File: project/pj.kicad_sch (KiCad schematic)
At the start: 11 parts, among them J1 RPi_GPIO, J2 2B+, J3 zero, J4 3A+, J5 3B+, J6 4, J7 Conn_01x02, J8 Conn_01x02, SW1 SW_Push, SW2 SW_Push

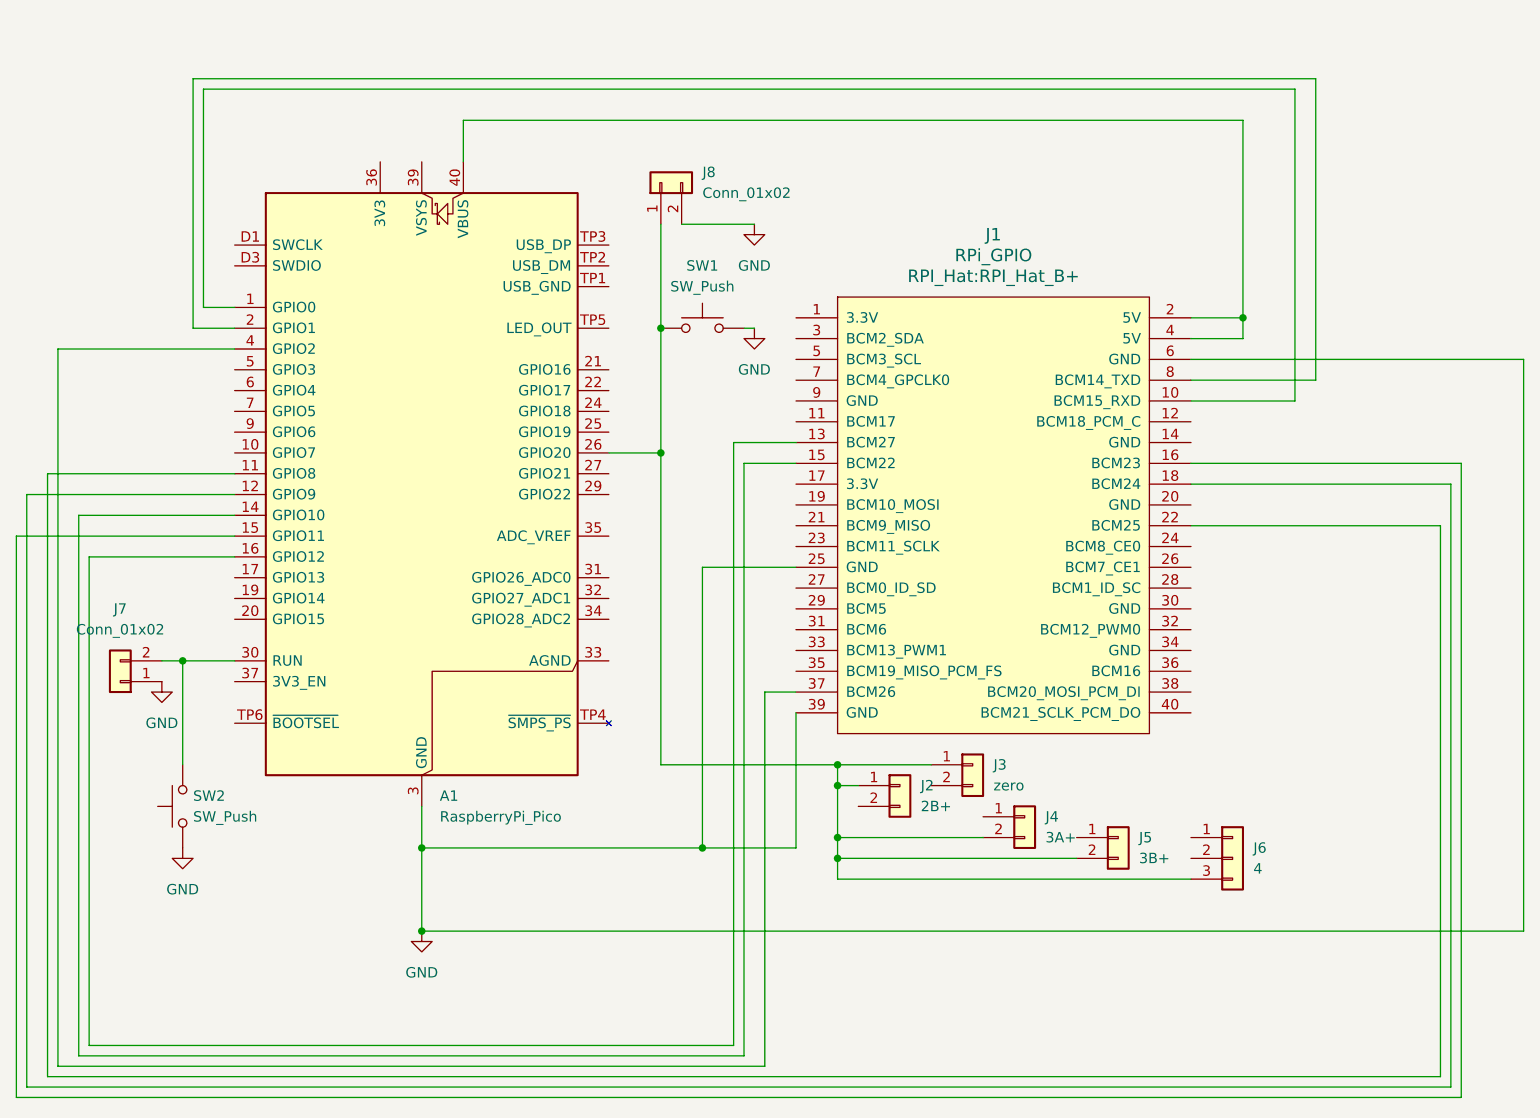
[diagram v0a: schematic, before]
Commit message: ground plane on both sides
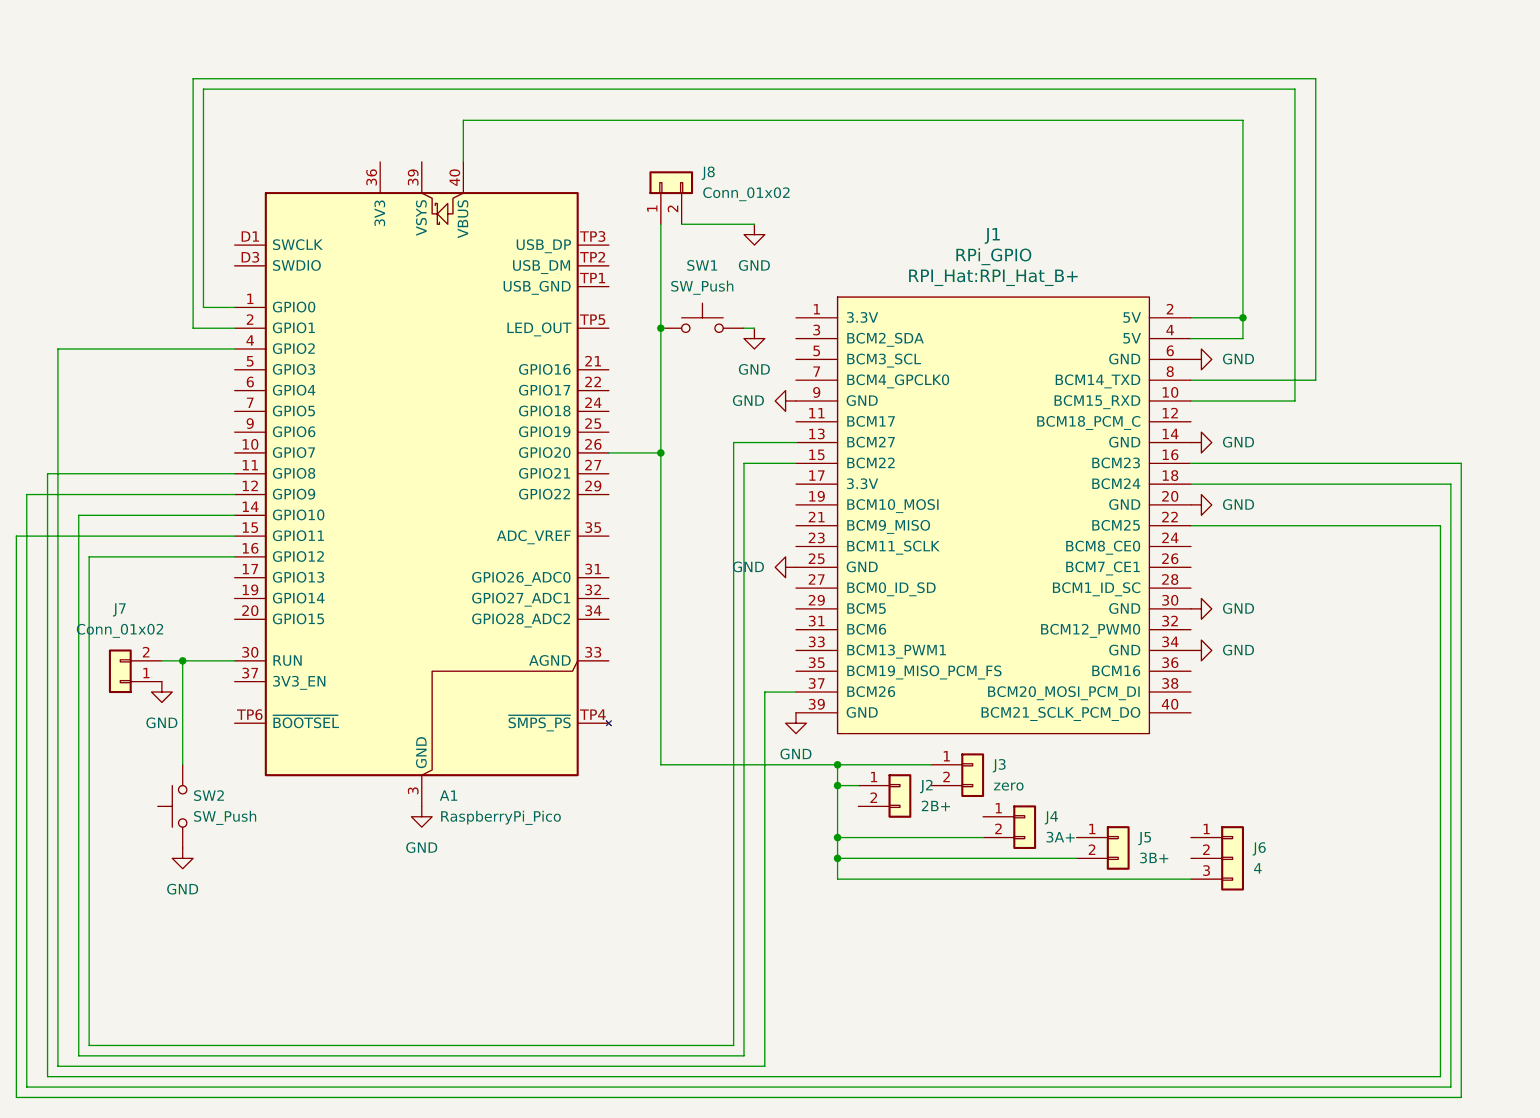
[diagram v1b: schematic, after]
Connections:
- net GND: now also J1.14 (GND), J1.20 (GND), J1.30 (GND), J1.34 (GND), J1.9 (GND)

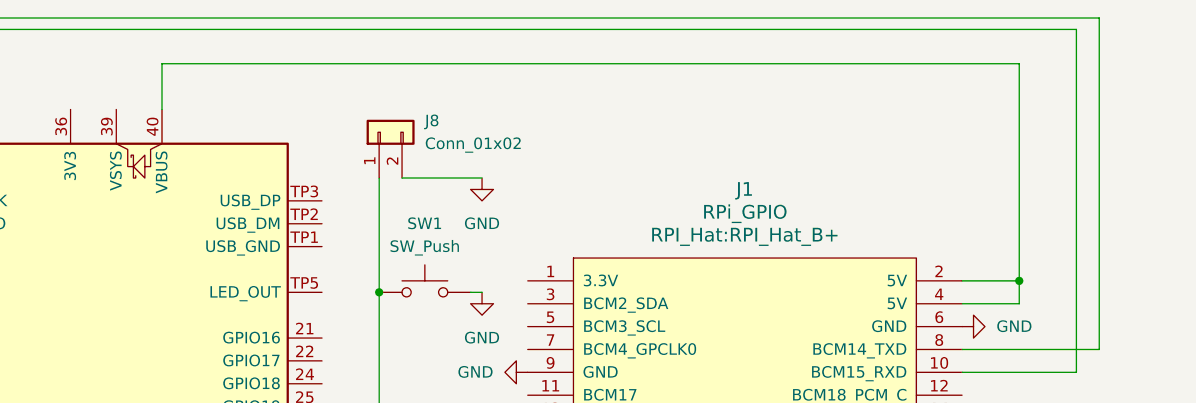
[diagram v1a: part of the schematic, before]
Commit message: Add Pico PWR and External PoWR
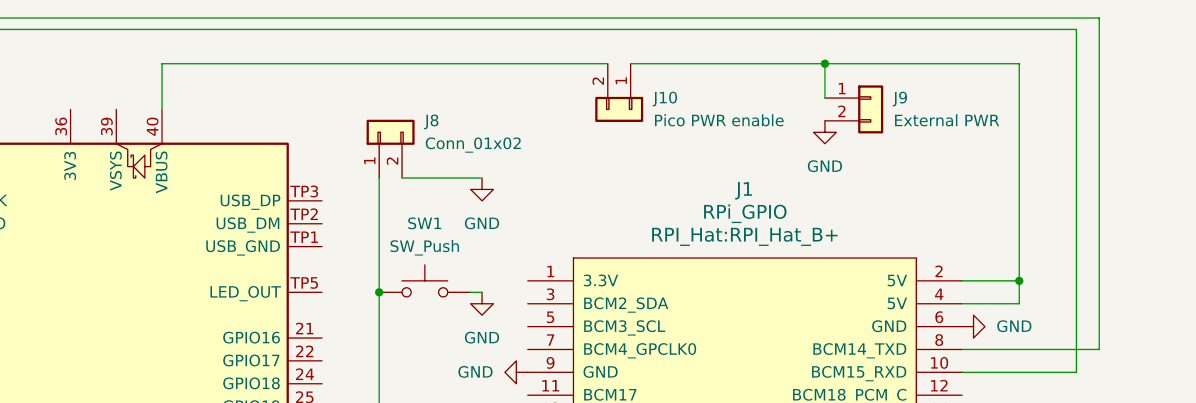
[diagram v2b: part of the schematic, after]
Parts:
- added J10: Pico PWR enable, symbol Connector_Generic:Conn_01x02
- added J9: External PWR, symbol Connector_Generic:Conn_01x02
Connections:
- net GND: now also J9.2 (Pin_2)
- net at J1.2 (5V), J1.4 (5V): now also J10.1 (Pin_1), J9.1 (Pin_1); no longer A1.40 (VBUS)
- new net: A1.40 (VBUS), J10.2 (Pin_2)
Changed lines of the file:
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@@
+	)
+	(junction
+		(at 165.1 31.75)
+		(diameter 0)
+		(color 0 0 0 0)
 	)
 	(junction
@@
 	(wire
 		(pts
+			(xy 165.1 35.56) (xy 165.1 31.75)
+		)
+		(stroke
+			(width 0)
+			(type default)
+		)
+	)
+	(wire
+		(pts
 			(xy 59.69 27.94) (xy 193.04 27.94)
 		)
@@
 	(wire
 		(pts
+			(xy 143.51 31.75) (xy 165.1 31.75)
+		)
+		(stroke
+			(width 0)
+			(type default)
+		)
+	)
+	(wire
+		(pts
 			(xy 38.1 77.47) (xy 63.5 77.47)
 		)
@@
 	(wire
 		(pts
+			(xy 165.1 31.75) (xy 186.69 31.75)
+		)
+		(stroke
+			(width 0)
+			(type default)
+		)
+	)
+	(wire
+		(pts
 			(xy 195.58 26.67) (xy 58.42 26.67)
 		)
@@
 	(wire
 		(pts
-			(xy 91.44 31.75) (xy 186.69 31.75)
+			(xy 91.44 31.75) (xy 140.97 31.75)
 		)
 		(stroke
@@
 	(symbol
 		(lib_id "power:GND")
+		(at 165.1 38.1 0)
+		(unit 1)
+		(exclude_from_sim no)
+		(in_bom yes)
+		(on_board yes)
+		(dnp no)
+		(fields_autoplaced yes)
+		(property "Reference" "#PWR014"
+			(at 165.1 44.45 0)
+			(effects
+				(font
+					(size 1.27 1.27)
+				)
+				(hide yes)
+			)
+		)
+		(property "Value" "GND"
+			(at 165.1 43.18 0)
+			(effects
+				(font
+					(size 1.27 1.27)
+				)
+			)
+		)
+		(property "Footprint" ""
+			(at 165.1 38.1 0)
+			(effects
+				(font
+					(size 1.27 1.27)
+				)
+				(hide yes)
+			)
+		)
+		(property "Datasheet" ""
+			(at 165.1 38.1 0)
+			(effects
+				(font
+					(size 1.27 1.27)
+				)
+				(hide yes)
+			)
+		)
+		(property "Description" "Power symbol creates a global label with name \"GND\" , ground"
+			(at 165.1 38.1 0)
+			(effects
+				(font
+					(size 1.27 1.27)
+				)
+				(hide yes)
+			)
+		)
+		(pin "1"
+		)
+		(instances
+			(project ""
+				(path "/3f830ea6-5a5f-4b7b-8d42-0620c39d4ee6"
+					(reference "#PWR014")
+					(unit 1)
+				)
+			)
+		)
+	)
+	(symbol
+		(lib_id "power:GND")
 		(at 57.15 120.65 0)
 		(unit 1)
@@
 	(symbol
 		(lib_id "Connector_Generic:Conn_01x02")
+		(at 170.18 35.56 0)
+		(unit 1)
+		(exclude_from_sim no)
+		(in_bom yes)
+		(on_board yes)
+		(dnp no)
+		(fields_autoplaced yes)
+		(property "Reference" "J9"
+			(at 172.72 35.5599 0)
+			(effects
+				(font
+					(size 1.27 1.27)
+				)
+				(justify left)
+			)
+		)
+		(property "Value" "External PWR"
+			(at 172.72 38.0999 0)
+			(effects
+				(font
+					(size 1.27 1.27)
+				)
+				(justify left)
+			)
+		)
+		(property "Footprint" ""
+			(at 170.18 35.56 0)
+			(effects
+				(font
+					(size 1.27 1.27)
+				)
+				(hide yes)
+			)
+		)
+		(property "Datasheet" "~"
+			(at 170.18 35.56 0)
+			(effects
+				(font
+					(size 1.27 1.27)
+				)
+				(hide yes)
+			)
+		)
+		(property "Description" "Generic connector, single row, 01x02, script generated (kicad-library-utils/schlib/autogen/connector/)"
+			(at 170.18 35.56 0)
+			(effects
+				(font
+					(size 1.27 1.27)
+				)
+				(hide yes)
+			)
+		)
+		(pin "1"
+		)
+		(pin "2"
+		)
+		(instances
+			(project ""
+				(path "/3f830ea6-5a5f-4b7b-8d42-0620c39d4ee6"
+					(reference "J9")
+					(unit 1)
+				)
+			)
+		)
+	)
+	(symbol
+		(lib_id "Connector_Generic:Conn_01x02")
 		(at 115.57 39.37 90)
 		(unit 1)
@@
 					(unit 1)
 				)
+			)
+		)
+	)
+	(symbol
+		(lib_id "Connector_Generic:Conn_01x02")
+		(at 143.51 36.83 270)
+		(unit 1)
+		(exclude_from_sim no)
+		(in_bom yes)
+		(on_board yes)
+		(dnp no)
+		(fields_autoplaced yes)
+		(property "Reference" "J10"
+			(at 146.05 35.5599 90)
+			(effects
+				(font
+					(size 1.27 1.27)
+				)
+				(justify left)
+			)
+		)
+		(property "Value" "Pico PWR enable"
+			(at 146.05 38.0999 90)
+			(effects
+				(font
+					(size 1.27 1.27)
+				)
+				(justify left)
+			)
+		)
+		(property "Footprint" ""
+			(at 143.51 36.83 0)
+			(effects
+				(font
+					(size 1.27 1.27)
+				)
+				(hide yes)
+			)
+		)
+		(property "Datasheet" "~"
+			(at 143.51 36.83 0)
+			(effects
+				(font
+					(size 1.27 1.27)
+				)
+				(hide yes)
+			)
+		)
+		(property "Description" "Generic connector, single row, 01x02, script generated (kicad-library-utils/schlib/autogen/connector/)"
+			(at 143.51 36.83 0)
+			(effects
+				(font
+					(size 1.27 1.27)
+				)
+				(hide yes)
+			)
+		)
+		(pin "2"
+		)
+		(pin "1"
+		)
+		(instances
+			(project ""
+				(path "/3f830ea6-5a5f-4b7b-8d42-0620c39d4ee6"
+					(reference "J10")
+					(unit 1)
+				)

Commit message: pwr eneble
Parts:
- J10: footprint (none) -> Jumper:SolderJumper-2_P1.3mm_Bridged2Bar_Pad1.0x1.5mm
- J9: footprint (none) -> Connector_PinHeader_1.27mm:PinHeader_1x02_P1.27mm_Vertical
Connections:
- net at J1.2 (5V), J1.4 (5V), J9.1 (Pin_1): now also J10.2 (Pin_2); no longer J10.1 (Pin_1)
- net at A1.40 (VBUS): now also J10.1 (Pin_1); no longer J10.2 (Pin_2)
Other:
- moved on the sheet: J10, J9
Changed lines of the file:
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@@
 	)
 	(junction
-		(at 165.1 31.75)
+		(at 166.37 35.56)
 		(diameter 0)
 		(color 0 0 0 0)
@@
 	(wire
 		(pts
-			(xy 165.1 35.56) (xy 165.1 31.75)
+			(xy 166.37 39.37) (xy 166.37 35.56)
 		)
 		(stroke
@@
 	(wire
 		(pts
-			(xy 143.51 31.75) (xy 165.1 31.75)
+			(xy 187.96 55.88) (xy 186.69 55.88)
+		)
+		(stroke
+			(width 0)
+			(type default)
+		)
+	)
+	(wire
+		(pts
+			(xy 144.78 35.56) (xy 166.37 35.56)
 		)
 		(stroke
@@
 	(wire
 		(pts
-			(xy 165.1 31.75) (xy 186.69 31.75)
+			(xy 166.37 35.56) (xy 187.96 35.56)
 		)
 		(stroke
@@
 	(wire
 		(pts
-			(xy 186.69 31.75) (xy 186.69 55.88)
+			(xy 187.96 35.56) (xy 187.96 55.88)
 		)
 		(stroke
@@
 	(wire
 		(pts
-			(xy 91.44 31.75) (xy 140.97 31.75)
+			(xy 91.44 35.56) (xy 142.24 35.56)
 		)
 		(stroke
@@
 	(wire
 		(pts
-			(xy 91.44 36.83) (xy 91.44 31.75)
+			(xy 91.44 36.83) (xy 91.44 35.56)
 		)
 		(stroke
@@
 	(symbol
 		(lib_id "power:GND")
-		(at 165.1 38.1 0)
+		(at 166.37 41.91 0)
 		(unit 1)
 		(exclude_from_sim no)
@@
 		(fields_autoplaced yes)
 		(property "Reference" "#PWR014"
-			(at 165.1 44.45 0)
+			(at 166.37 48.26 0)
 			(effects
 				(font
@@
 		)
 		(property "Value" "GND"
-			(at 165.1 43.18 0)
+			(at 166.37 46.99 0)
 			(effects
 				(font
@@
 		)
 		(property "Footprint" ""
-			(at 165.1 38.1 0)
+			(at 166.37 41.91 0)
 			(effects
 				(font
@@
 		)
 		(property "Datasheet" ""
-			(at 165.1 38.1 0)
+			(at 166.37 41.91 0)
 			(effects
 				(font
@@
 		)
 		(property "Description" "Power symbol creates a global label with name \"GND\" , ground"
-			(at 165.1 38.1 0)
+			(at 166.37 41.91 0)
 			(effects
 				(font
@@
 	(symbol
 		(lib_id "Connector_Generic:Conn_01x02")
-		(at 170.18 35.56 0)
+		(at 171.45 39.37 0)
 		(unit 1)
 		(exclude_from_sim no)
@@
 		(fields_autoplaced yes)
 		(property "Reference" "J9"
-			(at 172.72 35.5599 0)
+			(at 173.99 39.3699 0)
 			(effects
 				(font
@@
 		)
 		(property "Value" "External PWR"
-			(at 172.72 38.0999 0)
+			(at 173.99 41.9099 0)
 			(effects
 				(font
@@
 			)
 		)
-		(property "Footprint" ""
-			(at 170.18 35.56 0)
+		(property "Footprint" "Connector_PinHeader_1.27mm:PinHeader_1x02_P1.27mm_Vertical"
+			(at 171.45 39.37 0)
 			(effects
 				(font
@@
 		)
 		(property "Datasheet" "~"
-			(at 170.18 35.56 0)
+			(at 171.45 39.37 0)
 			(effects
 				(font
@@
 		)
 		(property "Description" "Generic connector, single row, 01x02, script generated (kicad-library-utils/schlib/autogen/connector/)"
-			(at 170.18 35.56 0)
+			(at 171.45 39.37 0)
 			(effects
 				(font
@@
 		(on_board yes)
 		(dnp no)
-		(fields_autoplaced yes)
 		(property "Reference" "J8"
 			(at 120.65 38.0999 90)
@@
 	(symbol
 		(lib_id "Connector_Generic:Conn_01x02")
-		(at 143.51 36.83 270)
+		(at 142.24 30.48 90)
 		(unit 1)
 		(exclude_from_sim no)
@@
 		(fields_autoplaced yes)
 		(property "Reference" "J10"
-			(at 146.05 35.5599 90)
-			(effects
-				(font
-					(size 1.27 1.27)
-				)
-				(justify left)
+			(at 147.32 29.2099 90)
+			(effects
+				(font
+					(size 1.27 1.27)
+				)
+				(justify right)
 			)
 		)
 		(property "Value" "Pico PWR enable"
-			(at 146.05 38.0999 90)
-			(effects
-				(font
-					(size 1.27 1.27)
-				)
-				(justify left)
-			)
-		)
-		(property "Footprint" ""
-			(at 143.51 36.83 0)
+			(at 147.32 31.7499 90)
+			(effects
+				(font
+					(size 1.27 1.27)
+				)
+				(justify right)
+			)
+		)
+		(property "Footprint" "Jumper:SolderJumper-2_P1.3mm_Bridged2Bar_Pad1.0x1.5mm"
+			(at 142.24 30.48 0)
 			(effects
 				(font
@@
 		)
 		(property "Datasheet" "~"
-			(at 143.51 36.83 0)
+			(at 142.24 30.48 0)
 			(effects
 				(font
@@
 		)
 		(property "Description" "Generic connector, single row, 01x02, script generated (kicad-library-utils/schlib/autogen/connector/)"
-			(at 143.51 36.83 0)
-			(effects
-				(font
+			(at 142.24 30.48 0)
+			(effects
+				(font

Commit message: beacon
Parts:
- added D1: Beacon, LED_SMD:LED_0603_1608Metric, symbol Device:LED
- added R1: 4.7k, Resistor_SMD:R_0603_1608Metric, symbol Device:R_Small
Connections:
- net GND: now also D1.1 (K)
- net at A1.2 (GPIO1): no longer J1.8 (BCM14_TXD)
- net at A1.29 (GPIO22): now also R1.2
- new net: D1.2 (A), R1.1
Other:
- note added: "DEBUG LED"
- moved on the sheet: J10, J8, J9, SW1
